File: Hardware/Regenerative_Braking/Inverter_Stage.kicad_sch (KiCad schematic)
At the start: 39 parts, among them IC1 IRS21867STRPBF, IC2 IRS21867STRPBF, IC3 IRS21867STRPBF

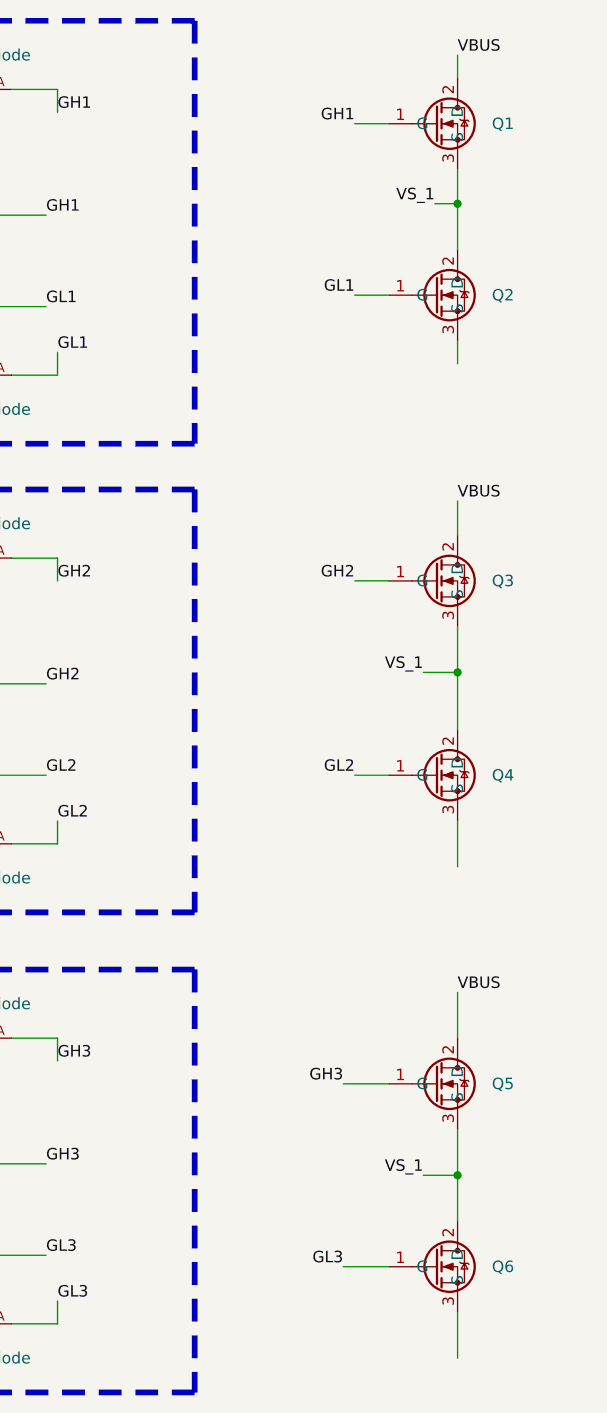
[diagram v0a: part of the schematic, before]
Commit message: edited till inverter circuit
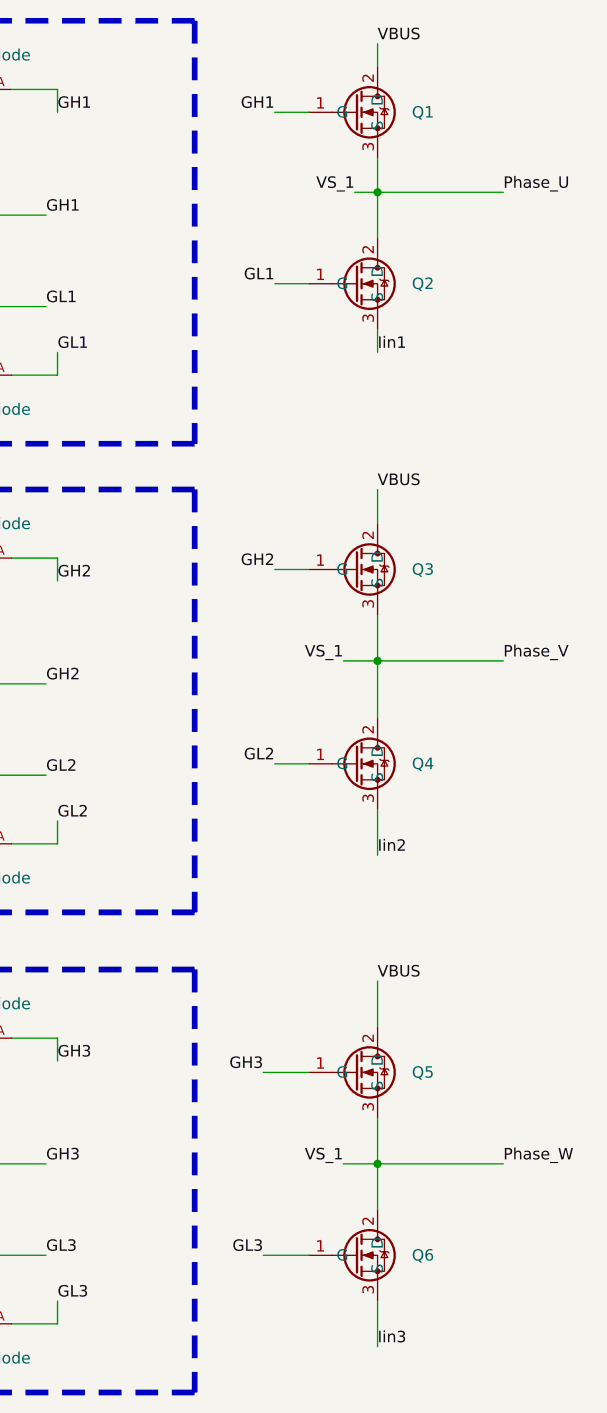
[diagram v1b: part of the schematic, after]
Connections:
- net Iin3: now reaches Q6.3 (S)
- net Iin2: now reaches Q4.3 (S)
- net Iin1: now reaches Q2.3 (S)
- net VS_1 renamed Phase_U
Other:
- moved on the sheet: Q1, Q2, Q3, Q4, Q5, Q6

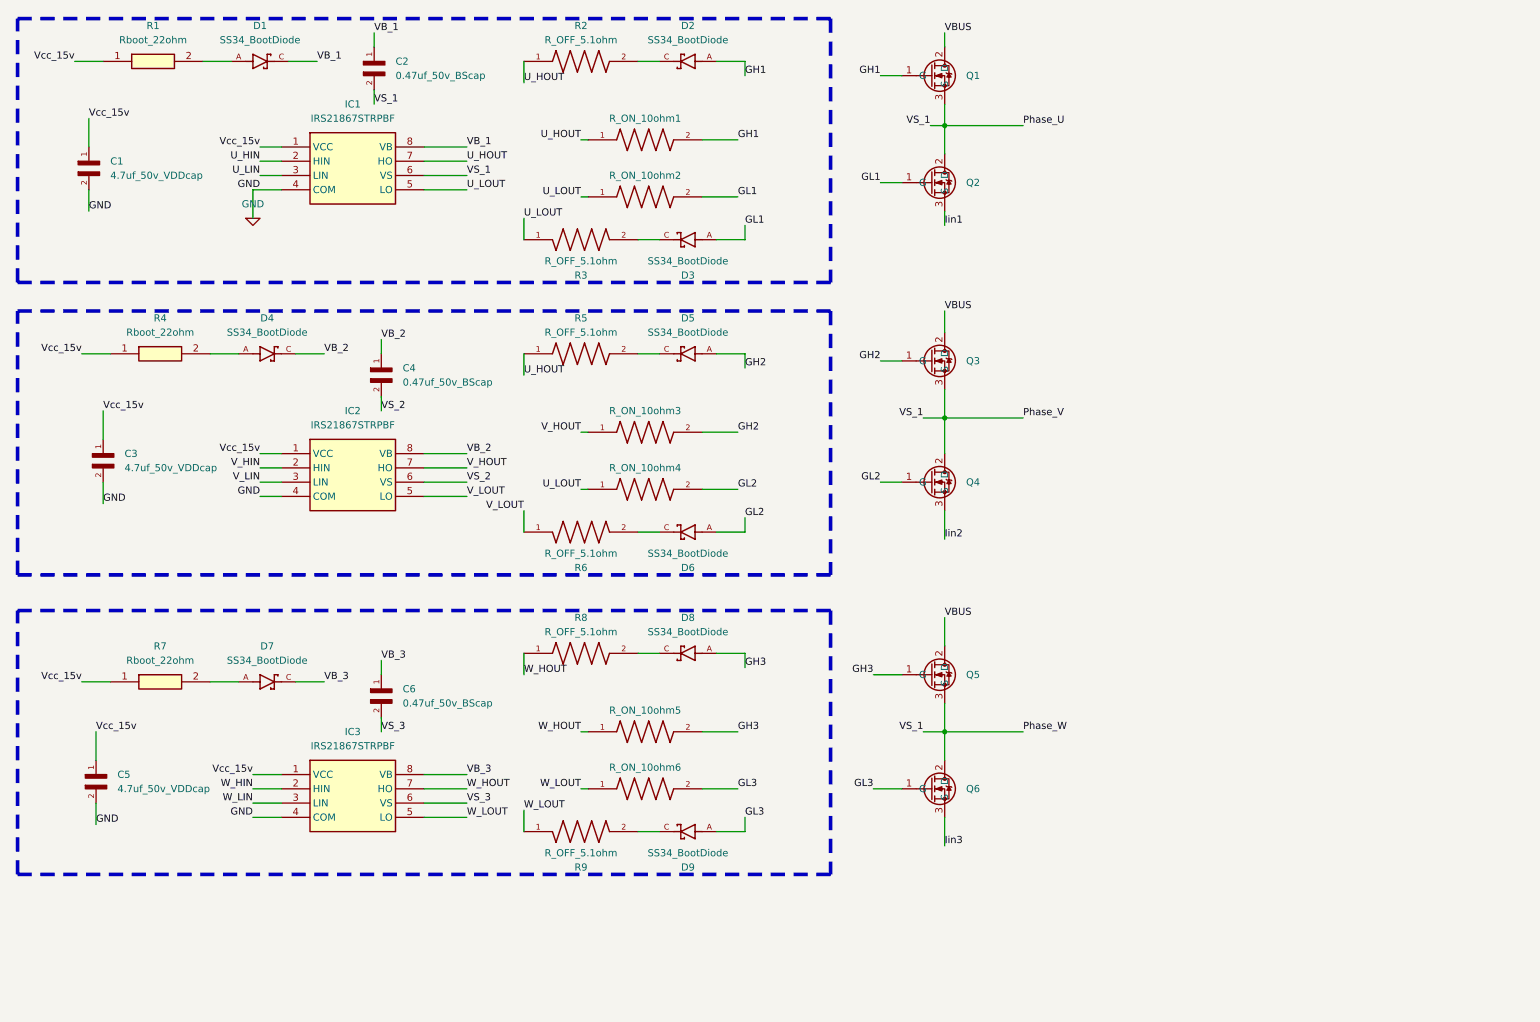
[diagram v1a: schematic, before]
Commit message: finished with sensing circuits & cap banks
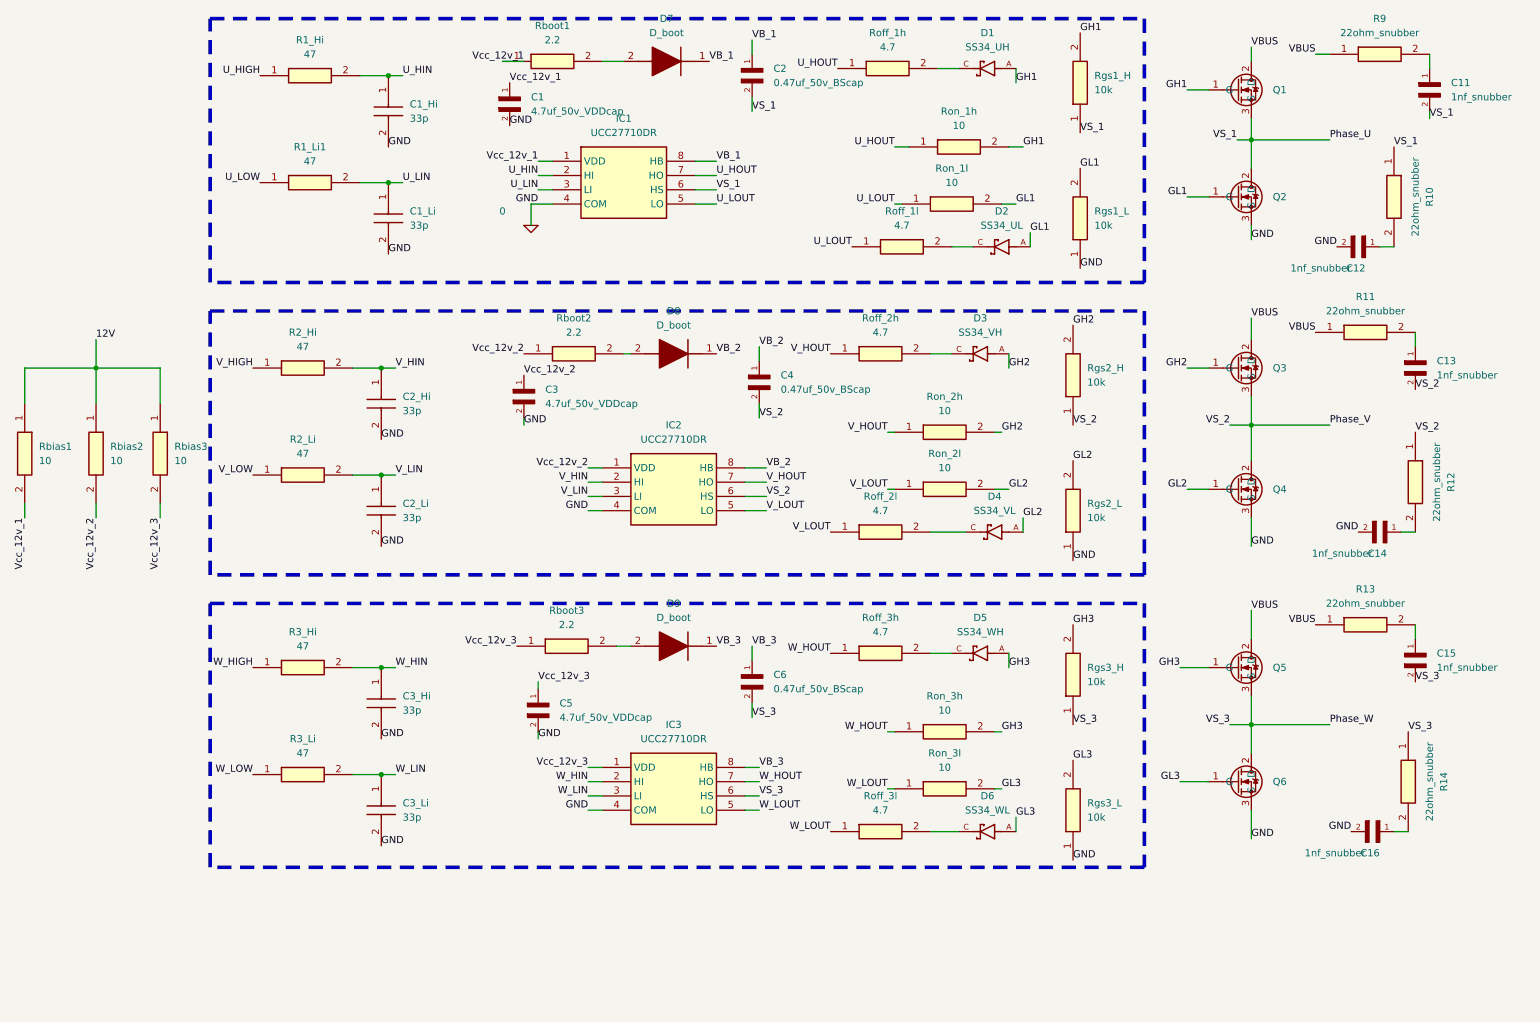
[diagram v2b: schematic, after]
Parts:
- removed D7, D8, D9: SS34_BootDiode, Regen_braking:boot_diode, symbol Regen_braking:SS34_BootDiode
- removed IC1, IC2, IC3: IRS21867STRPBF, Regen_braking:IRS21867STRPBF_gatedriver, symbol Regen_braking:IRS21867STRPBF
- removed R1, R4, R7: Rboot_22ohm, Regen_braking:Rboot_22ohm, symbol Regen_braking:Rboot_22ohm
- removed R2, R3, R5, R6, R8, R9: R_OFF_5.1ohm, Regen_braking:R_OFF_5.1ohm, symbol Regen_braking:R_OFF_5.1ohm
- removed R_ON_10ohm1, R_ON_10ohm2, R_ON_10ohm3, R_ON_10ohm4, R_ON_10ohm5, R_ON_10ohm6: (no value), Regen_braking:R_ON_10ohm, symbol Regen_braking:R_ON_10ohm
- added C11, C12, C13, C14, C15, C16: 1nf_snubber, Regen_braking:4.7uf_50v_VDDcap, symbol Regen_braking:1nf_snubber
- added C1_Hi, C1_Li, C2_Hi, C2_Li, C3_Hi, C3_Li: 33p, Regen_braking:33pf_ChiCli, symbol Regen_braking:33pf_ChiCli
- added D7, D8, D9: D_boot, Regen_braking:boot_diode, symbol Regen_braking:D_boot
- added IC1, IC2, IC3: UCC27710DR, Regen_braking:UCC27710DR, symbol Regen_braking:UCC27710DR
- added R10, R11, R12, R13, R14, R9: 22ohm_snubber, Regen_braking:Rboot_22ohm, symbol Regen_braking:22ohm_snubber
- added R1_Hi, R1_Li1, R2_Hi, R2_Li, R3_Hi, R3_Li: 47, Regen_braking:47,2.2,100k,10k,4.7,10ohm, symbol Regen_braking:47,2.2,100k,10k,4.7,10ohm
- added Rbias1, Rbias2, Rbias3, Ron_1h, Ron_1l, Ron_2h, Ron_2l, Ron_3h, Ron_3l: 10, Regen_braking:47,2.2,100k,10k,4.7,10ohm, symbol Regen_braking:47,2.2,100k,10k,4.7,10ohm
- added Rboot1, Rboot2, Rboot3: 2.2, Regen_braking:47,2.2,100k,10k,4.7,10ohm, symbol Regen_braking:47,2.2,100k,10k,4.7,10ohm
- added Rgs1_H, Rgs1_L, Rgs2_H, Rgs2_L, Rgs3_H, Rgs3_L: 10k, Regen_braking:47,2.2,100k,10k,4.7,10ohm, symbol Regen_braking:47,2.2,100k,10k,4.7,10ohm
- added Roff_1h, Roff_1l, Roff_2h, Roff_2l, Roff_3h, Roff_3l: 4.7, Regen_braking:47,2.2,100k,10k,4.7,10ohm, symbol Regen_braking:47,2.2,100k,10k,4.7,10ohm
- D1: value SS34_BootDiode -> SS34_UH; footprint Regen_braking:boot_diode -> Regen_braking:DIO_SS34
- D2: value SS34_BootDiode -> SS34_UL; footprint Regen_braking:boot_diode -> Regen_braking:DIO_SS34
- D3: value SS34_BootDiode -> SS34_VH; footprint Regen_braking:boot_diode -> Regen_braking:DIO_SS34
- D4: value SS34_BootDiode -> SS34_VL; footprint Regen_braking:boot_diode -> Regen_braking:DIO_SS34
- D5: value SS34_BootDiode -> SS34_WH; footprint Regen_braking:boot_diode -> Regen_braking:DIO_SS34
- D6: value SS34_BootDiode -> SS34_WL; footprint Regen_braking:boot_diode -> Regen_braking:DIO_SS34
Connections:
- net Iin1 is gone; now on net 0: Q2.3 (S)
- net Iin2 is gone; now on net 0: Q4.3 (S)
- net Iin3 is gone; now on net 0: Q6.3 (S)
- net GH1: now also D1.A, Rgs1_H.2, Ron_1h.2; no longer D2.A
- net GH2: now also D3.A, Rgs2_H.2, Ron_2h.2; no longer D5.A
- net GH3: now also D5.A, Rgs3_H.2, Ron_3h.2
- net GL1: now also D2.A, Rgs1_L.2, Ron_1l.2; no longer D3.A
- net GL2: now also D4.A, Rgs2_L.2, Ron_2l.2; no longer D6.A
- net GL3: now also D6.A, Rgs3_L.2, Ron_3l.2
- net Phase_U: now also C11.2, IC1.6 (HS), R10.1, Rgs1_H.1; no longer Q3.3 (S), Q4.2 (D), Q5.3 (S), Q6.2 (D)
- net U_HIN: now also C1_Hi.1, IC1.2 (HI), R1_Hi.2
- net U_HOUT: now also IC1.7 (HO), Roff_1h.1, Ron_1h.1
- net U_LIN: now also C1_Li.1, IC1.3 (LI), R1_Li1.2
- net U_LOUT: now also IC1.5 (LO), Roff_1l.1, Ron_1l.1
- net VBUS: now also R11.1, R13.1, R9.1
- net VB_1: now also D7.1 (K), IC1.8 (HB); no longer D1.C
- net VB_2: now also D8.1 (K), IC2.8 (HB); no longer D4.C
- net VB_3: now also D9.1 (K), IC3.8 (HB)
- net V_HIN: now also C2_Hi.1, IC2.2 (HI), R2_Hi.2
- net V_HOUT: now also IC2.7 (HO), Roff_2h.1, Ron_2h.1
- net V_LIN: now also C2_Li.1, IC2.3 (LI), R2_Li.2
- net V_LOUT: now also IC2.5 (LO), Roff_2l.1, Ron_2l.1
- net W_HIN: now also C3_Hi.1, IC3.2 (HI), R3_Hi.2
- net W_HOUT: now also IC3.7 (HO), Roff_3h.1, Ron_3h.1
- net W_LIN: now also C3_Li.1, IC3.3 (LI), R3_Li.2
- net W_LOUT: now also IC3.5 (LO), Roff_3l.1, Ron_3l.1
- net at D5.C: now also Roff_3h.2
- net at D2.C: now also Roff_1l.2
- net at D6.C: now also Roff_3l.2
- net at D3.C: now also Roff_2h.2
- net GND renamed 0
- net 0: now also C12.2, C14.2, C16.2, C1_Hi.2, C1_Li.2, C2_Hi.2, C2_Li.2, C3_Hi.2, C3_Li.2, IC1.4 (COM), IC2.4 (COM), IC3.4 (COM), Rgs1_L.1, Rgs2_L.1, Rgs3_L.1
- net VS_2 renamed Phase_V
- net Phase_V: now also Q3.3 (S), Q4.2 (D), C13.2, IC2.6 (HS), R12.1, Rgs2_H.1
- net VS_3 renamed Phase_W
- net Phase_W: now also Q5.3 (S), Q6.2 (D), C15.2, IC3.6 (HS), R14.1, Rgs3_H.1
- removed net Vcc_15v: C1.1, C3.1, C5.1
- new net: C11.1, R9.2
- new net: D9.2 (A), Rboot3.2
- new net: D7.2 (A), Rboot1.2
- new net: C15.1, R13.2
- new net: C16.1, R14.2
- new net: D4.C, Roff_2l.2
- new net: D1.C, Roff_1h.2
- new net: C14.1, R12.2
- new net: C13.1, R11.2
- new net: D8.2 (A), Rboot2.2
- new net: C12.1, R10.2
- new net 12V: Rbias1.1, Rbias2.1, Rbias3.1
- new net U_HIGH: R1_Hi.1
- new net U_LOW: R1_Li1.1
- new net V_HIGH: R2_Hi.1
- new net V_LOW: R2_Li.1
- new net Vcc_12v_1: C1.1, IC1.1 (VDD), Rbias1.2, Rboot1.1
- new net Vcc_12v_2: C3.1, IC2.1 (VDD), Rbias2.2, Rboot2.1
- new net Vcc_12v_3: C5.1, IC3.1 (VDD), Rbias3.2, Rboot3.1
- new net W_HIGH: R3_Hi.1
- new net W_LOW: R3_Li.1
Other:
- moved on the sheet: C1, C2, C3, C4, C5, C6, Q1, Q2, Q3, Q4, Q5, Q6

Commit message: finished schematic
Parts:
- removed C1_Li, C2_Hi, C2_Li, C3_Hi, C3_Li: 33p, Regen_braking:33pf_ChiCli, symbol Regen_braking:33pf_ChiCli
- removed R1_Li1, R2_Hi, R2_Li, R3_Hi, R3_Li: 47, Regen_braking:47,2.2,100k,10k,4.7,10ohm, symbol Regen_braking:47,2.2,100k,10k,4.7,10ohm
- removed Rboot2, Rboot3: 2.2, Regen_braking:47,2.2,100k,10k,4.7,10ohm, symbol Regen_braking:47,2.2,100k,10k,4.7,10ohm
- removed Rgs1_H, Rgs1_L, Rgs2_H, Rgs2_L, Rgs3_H, Rgs3_L: 10k, Regen_braking:47,2.2,100k,10k,4.7,10ohm, symbol Regen_braking:47,2.2,100k,10k,4.7,10ohm
- removed Roff_1l, Roff_2h, Roff_2l, Roff_3h, Roff_3l: 4.7, Regen_braking:47,2.2,100k,10k,4.7,10ohm, symbol Regen_braking:47,2.2,100k,10k,4.7,10ohm
- removed Ron_1l, Ron_2h, Ron_2l, Ron_3h, Ron_3l: 10, Regen_braking:47,2.2,100k,10k,4.7,10ohm, symbol Regen_braking:47,2.2,100k,10k,4.7,10ohm
- added C10, C42, C43, C44, C45: 33p, Capacitor_SMD:C_0805_2012Metric, symbol Regen_braking:33pf_ChiCli
- added R35, R37, R38, R39, R44: 47, Resistor_THT:R_Axial_DIN0207_L6.3mm_D2.5mm_P7.62mm_Horizontal, symbol Regen_braking:47,2.2,100k,10k,4.7,10ohm
- added R45, R46: 2.2, Resistor_THT:R_Axial_DIN0207_L6.3mm_D2.5mm_P7.62mm_Horizontal, symbol Regen_braking:47,2.2,100k,10k,4.7,10ohm
- added R47, R48, R49, R50, R51: 4.7, Resistor_THT:R_Axial_DIN0207_L6.3mm_D2.5mm_P7.62mm_Horizontal, symbol Regen_braking:47,2.2,100k,10k,4.7,10ohm
- added R52, R53, R54, R55, R56: 10, Resistor_THT:R_Axial_DIN0207_L6.3mm_D2.5mm_P7.62mm_Horizontal, symbol Regen_braking:47,2.2,100k,10k,4.7,10ohm
- added R57, R58, R59, R60, R61, R62: 10k, Resistor_THT:R_Axial_DIN0204_L3.6mm_D1.6mm_P7.62mm_Horizontal, symbol Regen_braking:47,2.2,100k,10k,4.7,10ohm
- C1: renamed from C1_Hi; footprint Regen_braking:33pf_ChiCli -> Capacitor_SMD:C_0805_2012Metric
- C11, C12, C13, C14, C15, C16: footprint Regen_braking:4.7uf_50v_VDDcap -> Capacitor_SMD:C_1206_3216Metric
- R1: renamed from Rboot1; footprint Regen_braking:47,2.2,100k,10k,4.7,10ohm -> Resistor_THT:R_Axial_DIN0207_L6.3mm_D2.5mm_P7.62mm_Horizontal
- R1: renamed from Ron_1h; footprint Regen_braking:47,2.2,100k,10k,4.7,10ohm -> Resistor_THT:R_Axial_DIN0207_L6.3mm_D2.5mm_P7.62mm_Horizontal
- R1: renamed from R1_Hi; footprint Regen_braking:47,2.2,100k,10k,4.7,10ohm -> Resistor_THT:R_Axial_DIN0207_L6.3mm_D2.5mm_P7.62mm_Horizontal
- R1: renamed from Roff_1h; footprint Regen_braking:47,2.2,100k,10k,4.7,10ohm -> Resistor_THT:R_Axial_DIN0207_L6.3mm_D2.5mm_P7.62mm_Horizontal
- Rbias1, Rbias2, Rbias3: footprint Regen_braking:47,2.2,100k,10k,4.7,10ohm -> Resistor_THT:R_Axial_DIN0207_L6.3mm_D2.5mm_P7.62mm_Horizontal
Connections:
- net 0: now also C13.2, C10.2, C42.2, C43.2, C44.2, C45.2, R58.2, R60.2, R62.2; no longer C16.2
- net GH1: now also R57.1
- net GH2: now also R53.2, R59.1
- net GH3: now also R55.2, R61.1
- net GL1: now also R52.2, R58.1
- net GL2: now also R54.2, R60.1
- net GL3: now also R56.2, R62.1
- net Phase_U: now also R57.2
- net Phase_V: now also C15.2, R59.2; no longer C13.2
- net Phase_W: now also C16.2, R61.2; no longer C15.2
- net U_LIN: now also C10.1, R35.2
- net U_LOUT: now also R47.1, R52.1
- net U_LOW: now also R35.1
- net V_HIGH: now also R37.1
- net V_HIN: now also C42.1, R37.2
- net V_HOUT: now also R48.1, R53.1
- net V_LIN: now also C43.1, R38.2
- net V_LOUT: now also R49.1, R54.1
- net V_LOW: now also R38.1
- net Vcc_12v_2: now also R45.1
- net Vcc_12v_3: now also R46.1
- net W_HIGH: now also R39.1
- net W_HIN: now also C44.1, R39.2
- net W_HOUT: now also R50.1, R55.1
- net W_LIN: now also C45.1, R44.2
- net W_LOUT: now also R51.1, R56.1
- net W_LOW: now also R44.1
- net at D5.C: now also R50.2
- net at D9.2 (A): now also R46.2
- net at D2.C: now also R47.2
- net at R13.2: now also C16.1; no longer C15.1
- net at R14.2: now also C14.1; no longer C16.1
- net at D3.C: now also R48.2
- net at D4.C: now also R49.2
- net at R12.2: now also C13.1; no longer C14.1
- net at R11.2: now also C15.1; no longer C13.1
- net at D6.C: now also R51.2
- net at D8.2 (A): now also R45.2
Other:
- moved on the sheet: R13

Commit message: finished placement
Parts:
- added J13: Conn_01x01, Connector_Wire:SolderWirePad_1x01_SMD_1.5x3mm, symbol Connector_Generic:Conn_01x01
- added J14: Screw_Terminal_01x03, Regen_braking:CUI_TB004-508-03BE, symbol Connector:Screw_Terminal_01x03
- added NT3, NT4, NT5: NetTie_4_Cross, NetTie:NetTie-4_SMD_Pad2.0mm, symbol Device:NetTie_4_Cross
- added Rbias4: 10, Resistor_THT:R_Axial_DIN0207_L6.3mm_D2.5mm_P7.62mm_Horizontal, symbol Regen_braking:47,2.2,100k,10k,4.7,10ohm
- R17: renamed from R9; footprint Regen_braking:Rboot_22ohm -> Resistor_THT:R_Axial_DIN0204_L3.6mm_D1.6mm_P7.62mm_Horizontal
- R20: renamed from R1; footprint Resistor_THT:R_Axial_DIN0207_L6.3mm_D2.5mm_P7.62mm_Horizontal -> Resistor_THT:R_Axial_DIN0204_L3.6mm_D1.6mm_P7.62mm_Horizontal
- R22: renamed from R10; footprint Regen_braking:Rboot_22ohm -> Resistor_THT:R_Axial_DIN0204_L3.6mm_D1.6mm_P7.62mm_Horizontal
- R24: renamed from R35; footprint Resistor_THT:R_Axial_DIN0207_L6.3mm_D2.5mm_P7.62mm_Horizontal -> Resistor_THT:R_Axial_DIN0204_L3.6mm_D1.6mm_P7.62mm_Horizontal
- R28: renamed from R11; footprint Regen_braking:Rboot_22ohm -> Resistor_THT:R_Axial_DIN0204_L3.6mm_D1.6mm_P7.62mm_Horizontal
- R31: renamed from R37; footprint Resistor_THT:R_Axial_DIN0207_L6.3mm_D2.5mm_P7.62mm_Horizontal -> Resistor_THT:R_Axial_DIN0204_L3.6mm_D1.6mm_P7.62mm_Horizontal
- R33: renamed from R12; footprint Regen_braking:Rboot_22ohm -> Resistor_THT:R_Axial_DIN0204_L3.6mm_D1.6mm_P7.62mm_Horizontal
- R35: renamed from R38; footprint Resistor_THT:R_Axial_DIN0207_L6.3mm_D2.5mm_P7.62mm_Horizontal -> Resistor_THT:R_Axial_DIN0204_L3.6mm_D1.6mm_P7.62mm_Horizontal
- R41: renamed from R13; footprint Regen_braking:Rboot_22ohm -> Resistor_THT:R_Axial_DIN0204_L3.6mm_D1.6mm_P7.62mm_Horizontal
- R42: renamed from R39; footprint Resistor_THT:R_Axial_DIN0207_L6.3mm_D2.5mm_P7.62mm_Horizontal -> Resistor_THT:R_Axial_DIN0204_L3.6mm_D1.6mm_P7.62mm_Horizontal
- R44: renamed from R14; footprint Regen_braking:Rboot_22ohm -> Resistor_THT:R_Axial_DIN0204_L3.6mm_D1.6mm_P7.62mm_Horizontal
- R46: renamed from R44; footprint Resistor_THT:R_Axial_DIN0207_L6.3mm_D2.5mm_P7.62mm_Horizontal -> Resistor_THT:R_Axial_DIN0204_L3.6mm_D1.6mm_P7.62mm_Horizontal
- renumbered C2 to C19, C1 to C20, C11 to C21, C1 to C22, C10 to C23, C12 to C24, C15 to C25, C42 to C26, C4 to C27, C3 to C28, C43 to C29, C13 to C30, C44 to C31, C6 to C32, C16 to C33, C5 to C34, C45 to C35, C14 to C36, D7 to D11, D1 to D12, D2 to D13, D8 to D14, D3 to D15, D4 to D16, D9 to D17, D5 to D18, D6 to D19, IC1 to IC2, IC2 to IC3, IC3 to IC4, Q1 to Q3, Q2 to Q4, Q3 to Q5, Q4 to Q6, Q5 to Q7, Q6 to Q8, R57 to R16, R1 to R18, R1 to R19, R1 to R21, R58 to R23, R52 to R25, R47 to R26, R59 to R27, R45 to R29, R48 to R30, R53 to R32, R60 to R34, R54 to R36, R49 to R37, R61 to R38, R46 to R39, R50 to R40, R55 to R43, R62 to R45, R56 to R47, R51 to R48
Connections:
- net 12V: now also J13.1 (Pin_1), Rbias4.1
- net Phase_U renamed VS_1
- net VS_1: now also NT3.1; no longer Q3.3 (S), Q4.2 (D)
- net Phase_V renamed VS_2
- net VS_2: now also NT4.1; no longer Q5.3 (S), Q6.2 (D)
- net Phase_W renamed VS_3
- net VS_3: now also NT5.1; no longer Q7.3 (S), Q8.2 (D)
- new net: NT5.4, Q8.2 (D)
- new net: NT5.3, Q7.3 (S)
- new net: NT3.3, Q3.3 (S)
- new net: NT4.3, Q5.3 (S)
- new net: NT3.4, Q4.2 (D)
- new net: NT4.4, Q6.2 (D)
- new net VDD: Rbias4.2
- no-connect marks 0 -> 6
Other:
- moved on the sheet: Rbias2, Rbias3

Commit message: ------------------Project Completed Successfully------------------
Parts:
- J13: value Conn_01x01 -> 12V
- J14: value Screw_Terminal_01x03 -> MOTOR_UVW
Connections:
- net VS_1: now also NT3.2
- net VS_2: now also NT4.2
- net VS_3: now also NT5.2
- net 0 renamed GND
- no-connect marks 6 -> 3
